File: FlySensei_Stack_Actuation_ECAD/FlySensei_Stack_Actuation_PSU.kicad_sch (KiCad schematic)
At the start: 26 parts, among them J5 JST_PH_SM2, SW1 SW_SPDT, U6 MPM3610, U7 MPM3610, U8 MAX17048G+T10

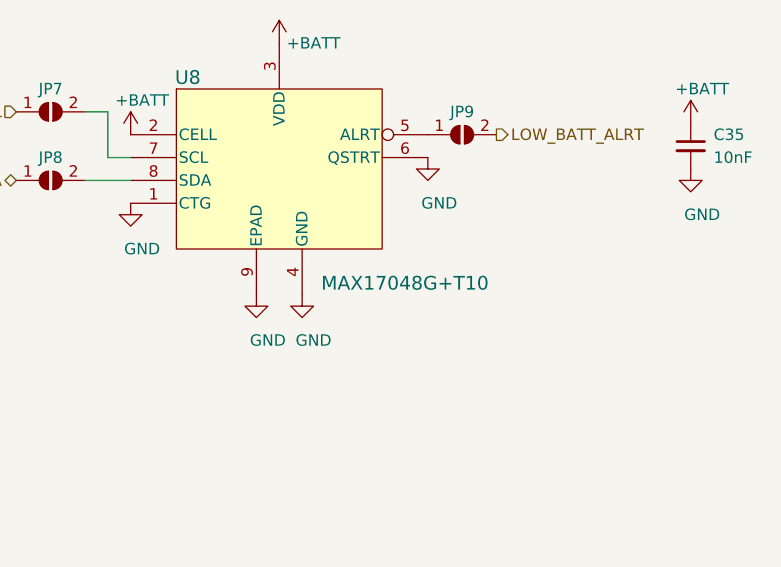
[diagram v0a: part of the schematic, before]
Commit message: Update part number for fuel gauge IC
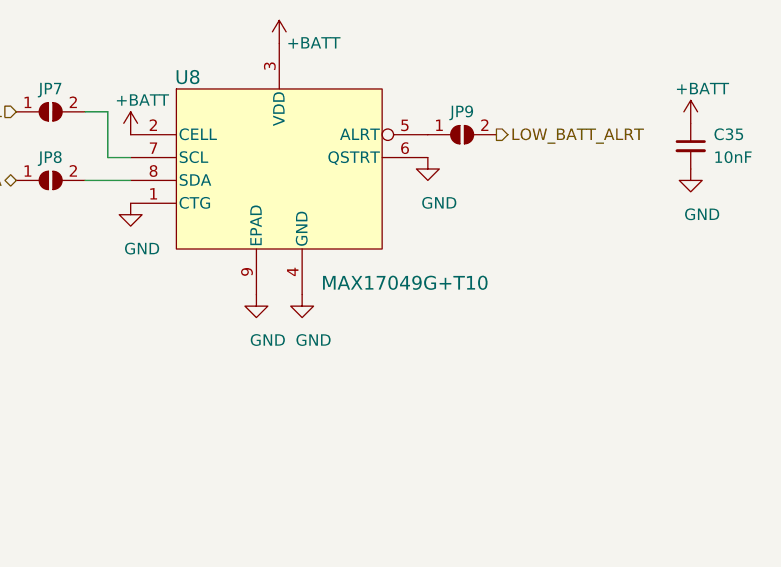
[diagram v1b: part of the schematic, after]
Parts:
- U8: value MAX17048G+T10 -> MAX17049G+T10
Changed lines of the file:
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@@
       (effects (font (size 1.524 1.524)))
     )
-    (property "Value" "MAX17048G+T10" (id 1) (at 218.44 97.79 0)
+    (property "Value" "MAX17049G+T10" (id 1) (at 218.44 97.79 0)
       (effects (font (size 1.524 1.524)))
     )

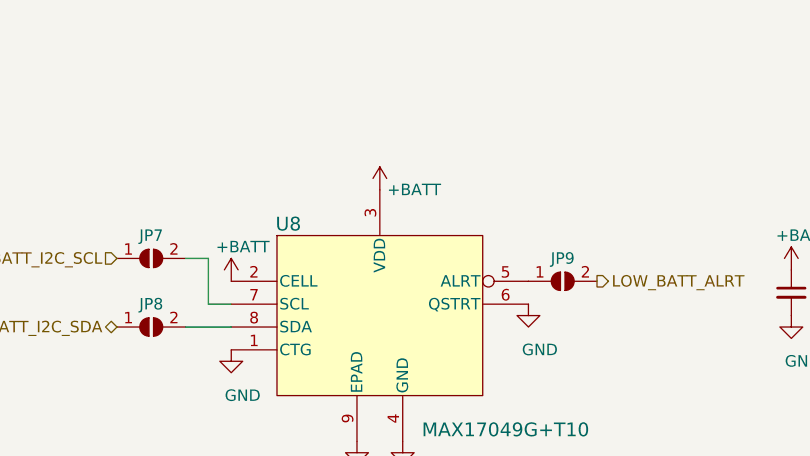
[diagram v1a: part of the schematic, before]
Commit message: Change PWM generation IC package to TSSOP due to availibility
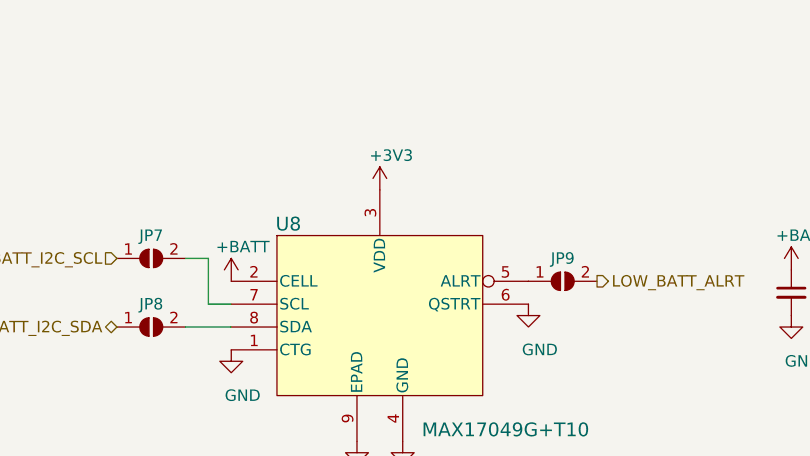
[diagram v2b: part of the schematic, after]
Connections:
- net +3V3: now also U8.3 (VDD)
- net +BATT: no longer U8.3 (VDD)
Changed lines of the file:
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@@
-(kicad_sch (version 20210406) (generator eeschema)
+(kicad_sch (version 20210606) (generator eeschema)
   (paper "A4")
   (junction (at 139.7 71.12) (diameter 1.016) (color 0 0 0 0))
@@
     (pin "1")
   )
-  (symbol (lib_id "power:+BATT") (at 204.47 71.12 0) (unit 1)
-    (in_bom yes) (on_board yes)
-    (property "Reference" "#PWR0247" (id 0) (at 204.47 74.93 0)
-      (effects (font (size 1.27 1.27)) hide)
-    )
-    (property "Value" "+BATT" (id 1) (at 208.28 71.12 0))
+  (symbol (lib_id "power:+3V3") (at 204.47 71.12 0) (unit 1)
+    (in_bom yes) (on_board yes)
+    (property "Reference" "#PWR?" (id 0) (at 204.47 74.93 0)
+      (effects (font (size 1.27 1.27)) hide)
+    )
+    (property "Value" "+3V3" (id 1) (at 205.74 67.31 0))
     (property "Footprint" "" (id 2) (at 204.47 71.12 0)
       (effects (font (size 1.27 1.27)) hide)
